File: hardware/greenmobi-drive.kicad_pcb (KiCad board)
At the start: 2 copper layers, 100 x 100 mm, 165 parts, among them J101 UBAT, J102 GND, J103 Encoder/Hall, J104 Motor NTC, J105 USB_C_Receptacle_USB2.0_14P, J106 CAN, J107 ADC, J108 ADC, J201 Debug, J301 Phase_OUT, J401 Phase_OUT, J501 Phase_OUT, Q301 IPT015N10N5, Q302 IPT015N10N5, Q401 IPT015N10N5, Q402 IPT015N10N5, Q501 IPT015N10N5, Q502 IPT015N10N5, SW201 BOOT, SW202 RESET, U101 BMI323, U102 TJA1051T-3, U201 STM32F405RGTx, U301 IRS21867S, U302 INA240A2D, U401 IRS21867S, U402 INA240A2D, U501 IRS21867S, U502 INA240A2D, U601 TPS54202DDC, U602 LM5163DDA, U603 AMS1117-3.3, Y201 8MHz

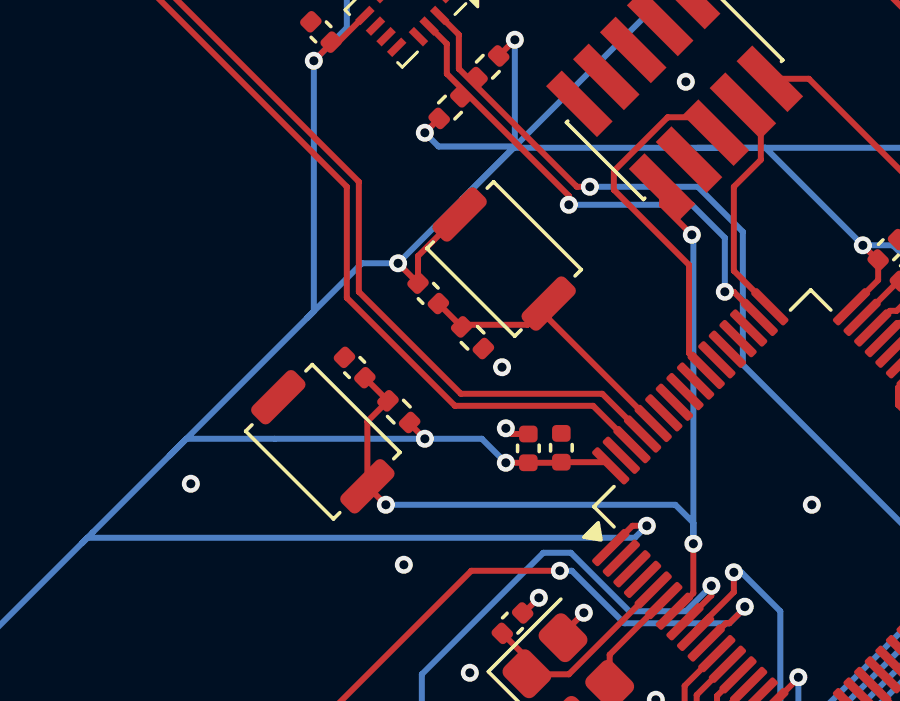
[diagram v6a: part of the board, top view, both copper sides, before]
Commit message: Removed buttons for boot and reset
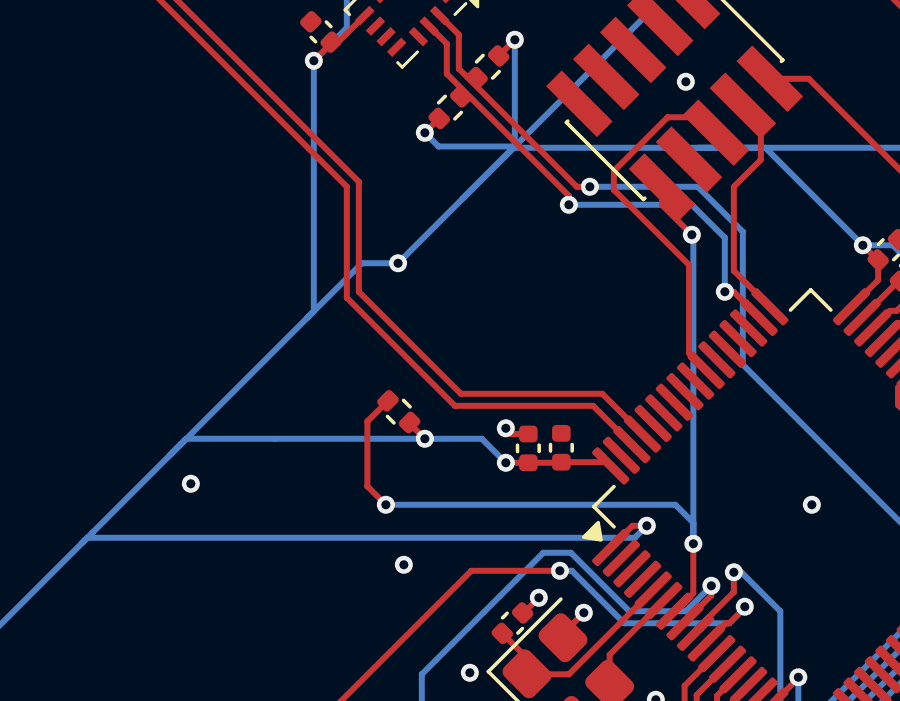
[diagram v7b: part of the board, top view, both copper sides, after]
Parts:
- removed C201, C202: 100n, Capacitor_SMD:C_0402_1005Metric
- removed R202: 5.1k, Resistor_SMD:R_0402_1005Metric
- removed SW201: BOOT, Button_Switch_SMD:SW_Push_SPST_NO_Alps_SKRK
- removed SW202: RESET, Button_Switch_SMD:SW_Push_SPST_NO_Alps_SKRK
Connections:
- R201 pad 2: /mcu/RESET -> Net-(U201-NRST)
- U201 pad 60: /mcu/BOOT -> GND
- U201 pad 7: /mcu/RESET -> Net-(U201-NRST)
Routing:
- net /mcu/BOOT: track 9.76 -> 0.00 mm
- net +3.3V: track 318.9 -> 315.1 mm
- net /mcu/RESET: track 31.1 -> 30.0 mm
- net GND: vias 72 -> 71

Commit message: Changed bootstrap resistor to 0 Ohm
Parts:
- D101: value SM6T56A -> SMBJ58A
- R301, R401, R501: value 4.7 -> 0
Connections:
- R201 pad 2: Net-(U201-NRST) -> /mcu/RESET
- U201 pad 7: Net-(U201-NRST) -> /mcu/RESET
